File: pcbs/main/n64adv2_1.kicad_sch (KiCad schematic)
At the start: 74 parts, among them Q1 2N2222, Q2 2N2222, Q3 2N2222, U1 10M16SCE144/10M25SCE144, U2 ADV7513, U3 MT48LC16M16A2-TSOP54, U4 SI5356DIY, U5 ASE-50.000MHZ-LC-T, U6 ASE-24.576MHZ-LC-T, U7 2G17TI_DBV, X1 Conn_01x30, X2 2510-, X3 hdmi-con, X4 TEI0005, X5 USB3140-30-0170-0-C, Y41 7A-27.000MAAJ-T

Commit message: update main PCB with minor changes, e.g. ensure that solder mask bridges between 0.5mm pitched pads has min. 0.1mm thickness
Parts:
- ALRCLK1, ASCLK1, ASDATA1, CTRL1, VD0, VD1, VD2, VD3, VD4, VD5, VD6, VDCLK1, nRST1, nVDS1, nViDeBlur1: value (none) -> SMD1; footprint (none) -> n64adv2:SMD0,8-1,6
- D23: value (none) -> NUP4114; footprint (none) -> n64adv2:SOT-23-6
- SJ11, SJ31, SJ5, SJ6: value (none) -> SJSMALL; footprint (none) -> n64adv2:SJ_SMALL
- TP_SCL0, TP_SDA0, TP_SPDIF0: value (none) -> TPB1,27; footprint (none) -> n64adv2:B1,27
- U3: value MT48LC16M16A2-TSOP54 -> AS4C8M16SA-xTCN
- U4: value SI5356DIY -> SI5356A-B-GMR
- U7: value 2G17TI_DBV -> 74LVC2G17DBV
- X2: value 2510- -> 3020-10-0300-00

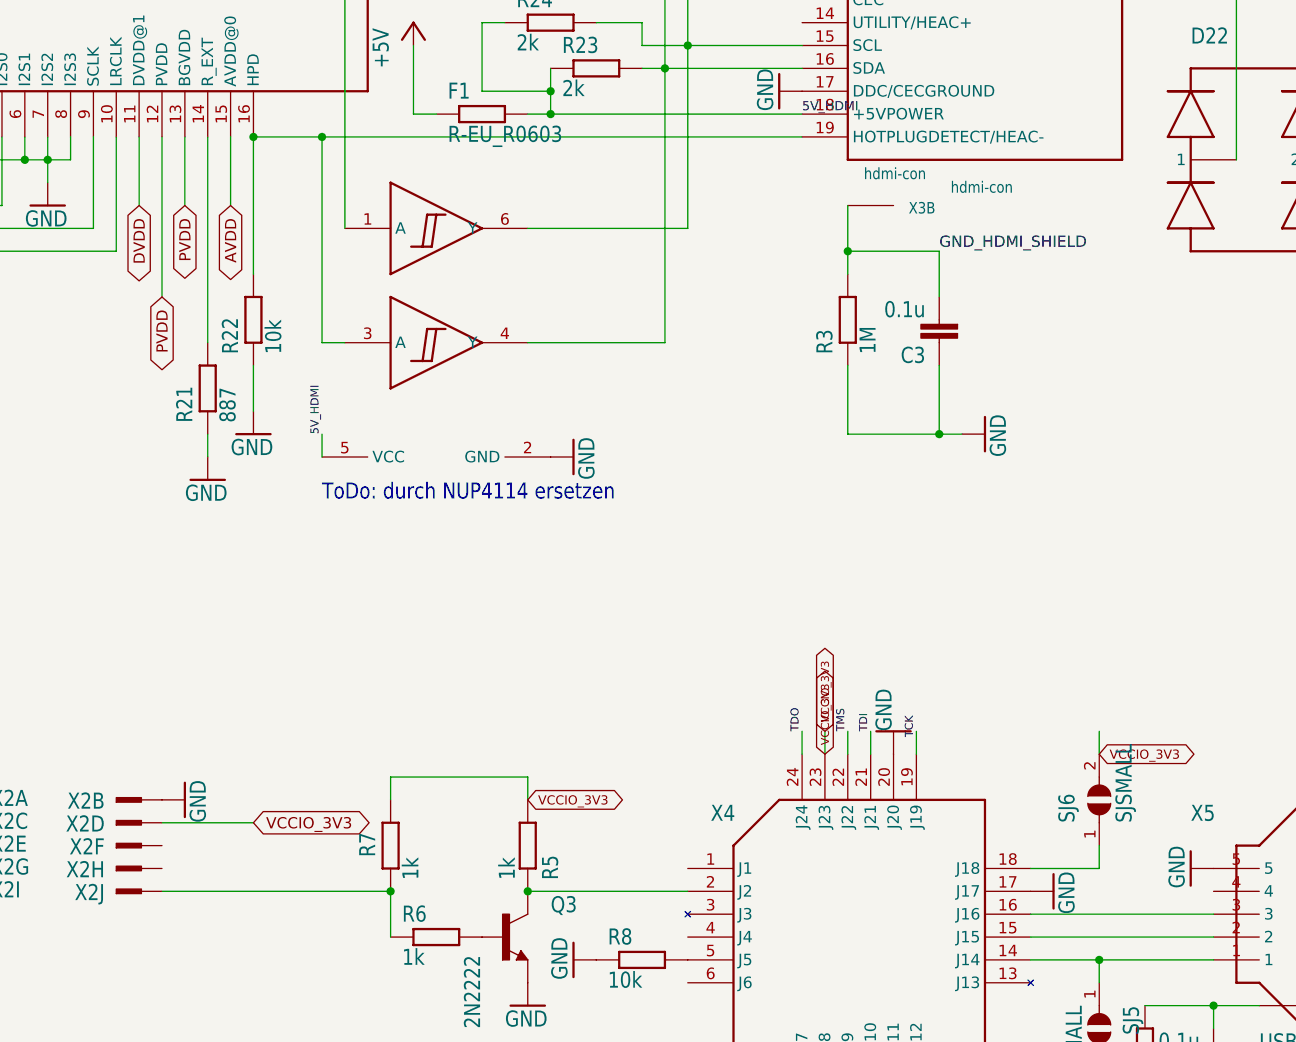
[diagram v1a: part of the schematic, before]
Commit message: update main PCB: - optimize some trace routing - optimize component selection/placing (e.g. HDMI port full SMD, JTAG as SMD alternative) - add license to silkscreen
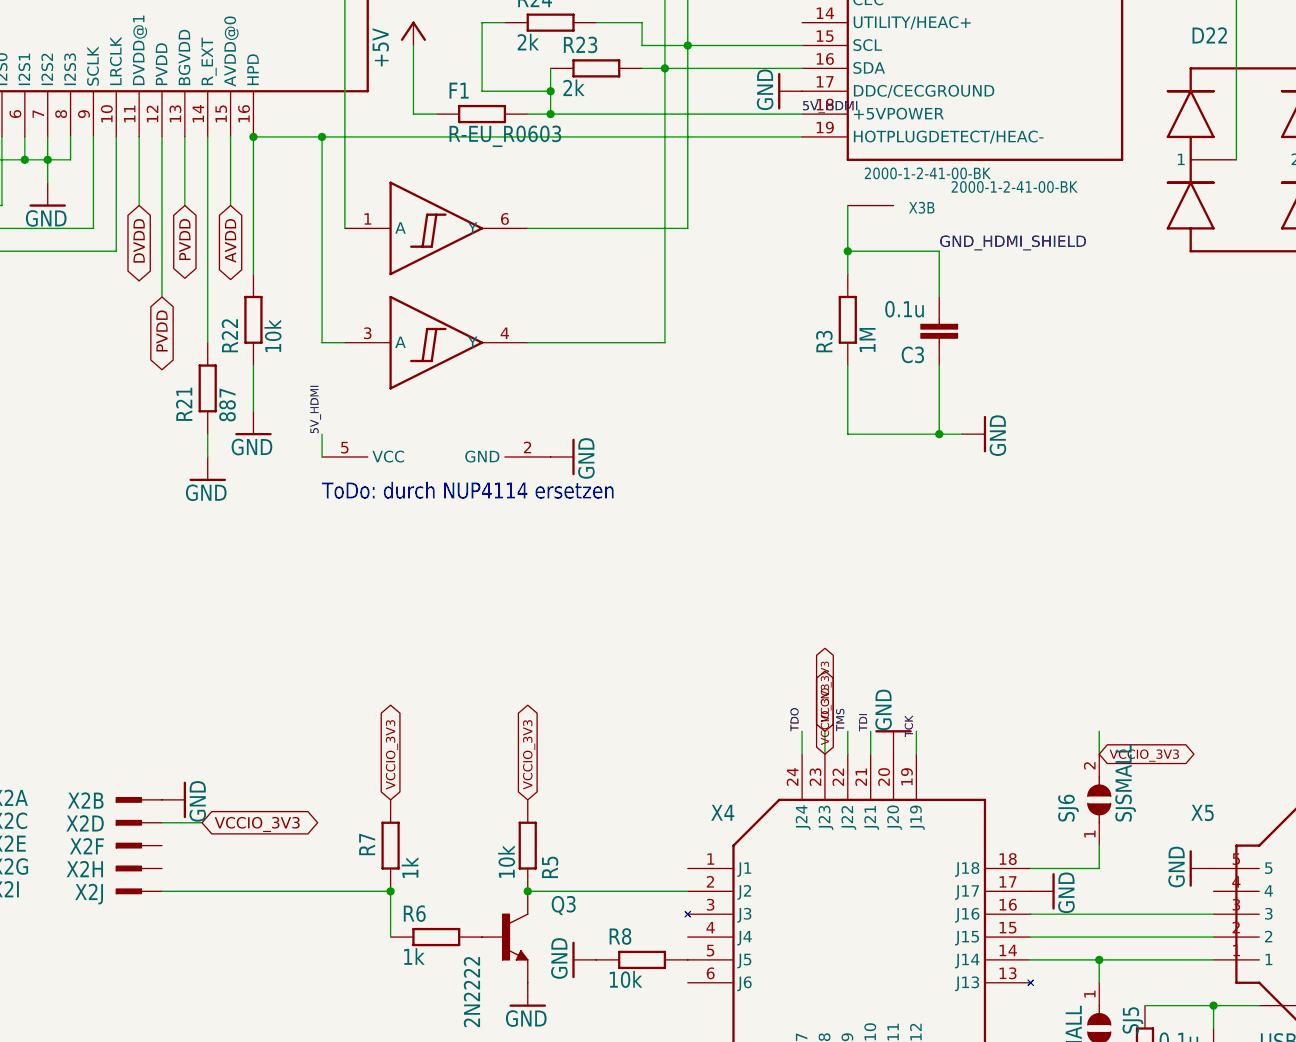
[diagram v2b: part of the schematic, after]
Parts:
- R5: value 1k -> 10k
- X3: value hdmi-con -> 2000-1-2-41-00-BK; footprint n64adv2:685119134923 -> n64adv2:hdmi_smd_shield_2000-1-2-41-00-BK
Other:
- company: (none) -> Peter 'borti4938' Bartmann
- title: (none) -> N64Adv2 (ADV7513)
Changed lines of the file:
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@@
 (kicad_sch (version 20211123) (generator eeschema)
   (paper "User" 783.336 357.353)
+  (title_block
+    (title "N64Adv2 (ADV7513)")
+    (rev "v20220729")
+    (company "Peter 'borti4938' Bartmann")
+    (comment 1 "Schematic and PCB (c) 2021, 2022 by Peter Bartmann")
+    (comment 2 "N64Adv2_20220729")
+    (comment 3 "Licensed under CERN-OHL-W v2")
+  )
   (junction (at 332.74 302.26) (diameter 0) (color 0 0 0 0)
   )
@@
     (stroke (width 0) (type default) (color 0 0 0 0))
   )
-  (wire (pts (xy 604.52 208.28) (xy 604.52 205.74))
-    (stroke (width 0) (type default) (color 0 0 0 0))
-  )
   (wire (pts (xy 292.1 231.14) (xy 320.04 231.14))
     (stroke (width 0) (type default) (color 0 0 0 0))
@@
     (stroke (width 0) (type default) (color 0 0 0 0))
   )
-  (wire (pts (xy 619.76 205.74) (xy 604.52 205.74))
-    (stroke (width 0) (type default) (color 0 0 0 0))
-  )
   (wire (pts (xy 655.32 147.32) (xy 655.32 142.24))
     (stroke (width 0) (type default) (color 0 0 0 0))
@@
     (stroke (width 0) (type default) (color 0 0 0 0))
   )
-  (wire (pts (xy 579.12 210.82) (xy 589.28 210.82))
-    (stroke (width 0) (type default) (color 0 0 0 0))
-  )
   (wire (pts (xy 563.88 60.96) (xy 563.88 33.02))
     (stroke (width 0) (type default) (color 0 0 0 0))
@@
     (stroke (width 0) (type default) (color 0 0 0 0))
   )
-  (wire (pts (xy 619.76 208.28) (xy 619.76 205.74))
-    (stroke (width 0) (type default) (color 0 0 0 0))
-  )
   (wire (pts (xy 683.26 203.2) (xy 683.26 200.66))
     (stroke (width 0) (type default) (color 0 0 0 0))
@@
     (stroke (width 0) (type default) (color 0 0 0 0))
   )
+  (wire (pts (xy 579.12 210.82) (xy 583.565 210.82))
+    (stroke (width 0) (type default) (color 0 0 0 0))
+  )
   (wire (pts (xy 205.74 111.76) (xy 198.12 111.76))
     (stroke (width 0) (type default) (color 0 0 0 0))
@@
     )
   )
-  (global_label "VCCIO_3V3" (shape bidirectional) (at 619.76 208.28 0) (fields_autoplaced)
+  (global_label "VCCIO_3V3" (shape bidirectional) (at 619.76 208.28 90) (fields_autoplaced)
     (effects (font (size 1.016 1.016)) (justify left))
-    (property "Intersheet References" "${INTERSHEET_REFS}" (id 0) (at 0 0 0)
+    (property "Intersheet References" "${INTERSHEET_REFS}" (id 0) (at 411.48 828.04 0)
       (effects (font (size 1.27 1.27)) hide)
     )
@@
     )
   )
+  (global_label "VCCIO_3V3" (shape bidirectional) (at 604.52 208.28 90) (fields_autoplaced)
+    (effects (font (size 1.016 1.016)) (justify left))
+    (property "Intersheet References" "${INTERSHEET_REFS}" (id 0) (at 396.24 828.04 0)
+      (effects (font (size 1.27 1.27)) hide)
+    )
+  )
   (global_label "U7_2V5" (shape bidirectional) (at 416.56 172.72 90) (fields_autoplaced)
     (effects (font (size 0.889 0.889)) (justify left))
@@
     )
   )
-  (global_label "VCCIO_3V3" (shape bidirectional) (at 589.28 210.82 0) (fields_autoplaced)
+  (global_label "VCCIO_3V3" (shape bidirectional) (at 583.565 210.82 0) (fields_autoplaced)
     (effects (font (size 1.2446 1.2446)) (justify left))
-    (property "Intersheet References" "${INTERSHEET_REFS}" (id 0) (at 0 0 0)
+    (property "Intersheet References" "${INTERSHEET_REFS}" (id 0) (at -5.715 0 0)
       (effects (font (size 1.27 1.27)) hide)
     )
@@
       (effects (font (size 1.27 1.0795)) (justify left bottom))
     )
-    (property "Value" "hdmi-con" (id 1) (at 666.75 140.97 0)
+    (property "Value" "2000-1-2-41-00-BK" (id 1) (at 666.75 140.97 0)
       (effects (font (size 1.27 1.0795)) (justify left bottom))
     )
-    (property "Footprint" "n64adv2:685119134923" (id 2) (at 670.56 111.76 0)
+    (property "Footprint" "n64adv2:hdmi_smd_shield_2000-1-2-41-00-BK" (id 2) (at 670.56 111.76 0)
       (effects (font (size 1.27 1.27)) hide)
     )
@@
       (effects (font (size 1.27 1.0795)) (justify left bottom))
     )
-    (property "Value" "hdmi-con" (id 1) (at 657.1 139.46 0)
+    (property "Value" "2000-1-2-41-00-BK" (id 1) (at 657.1 139.46 0)
       (effects (font (size 1.27 1.0795)) (justify left bottom))
     )
-    (property "Footprint" "n64adv2:685119134923" (id 2) (at 660.4 142.24 0)
+    (property "Footprint" "n64adv2:hdmi_smd_shield_2000-1-2-41-00-BK" (id 2) (at 660.4 142.24 0)
       (effects (font (size 1.27 1.27)) hide)
     )
@@
       (effects (font (size 1.778 1.5113)) (justify left bottom))
     )
-    (property "Value" "1k" (id 1) (at 616.458 217.17 0)
+    (property "Value" "10k" (id 1) (at 616.458 217.17 0)
       (effects (font (size 1.778 1.5113)) (justify left bottom))
     )

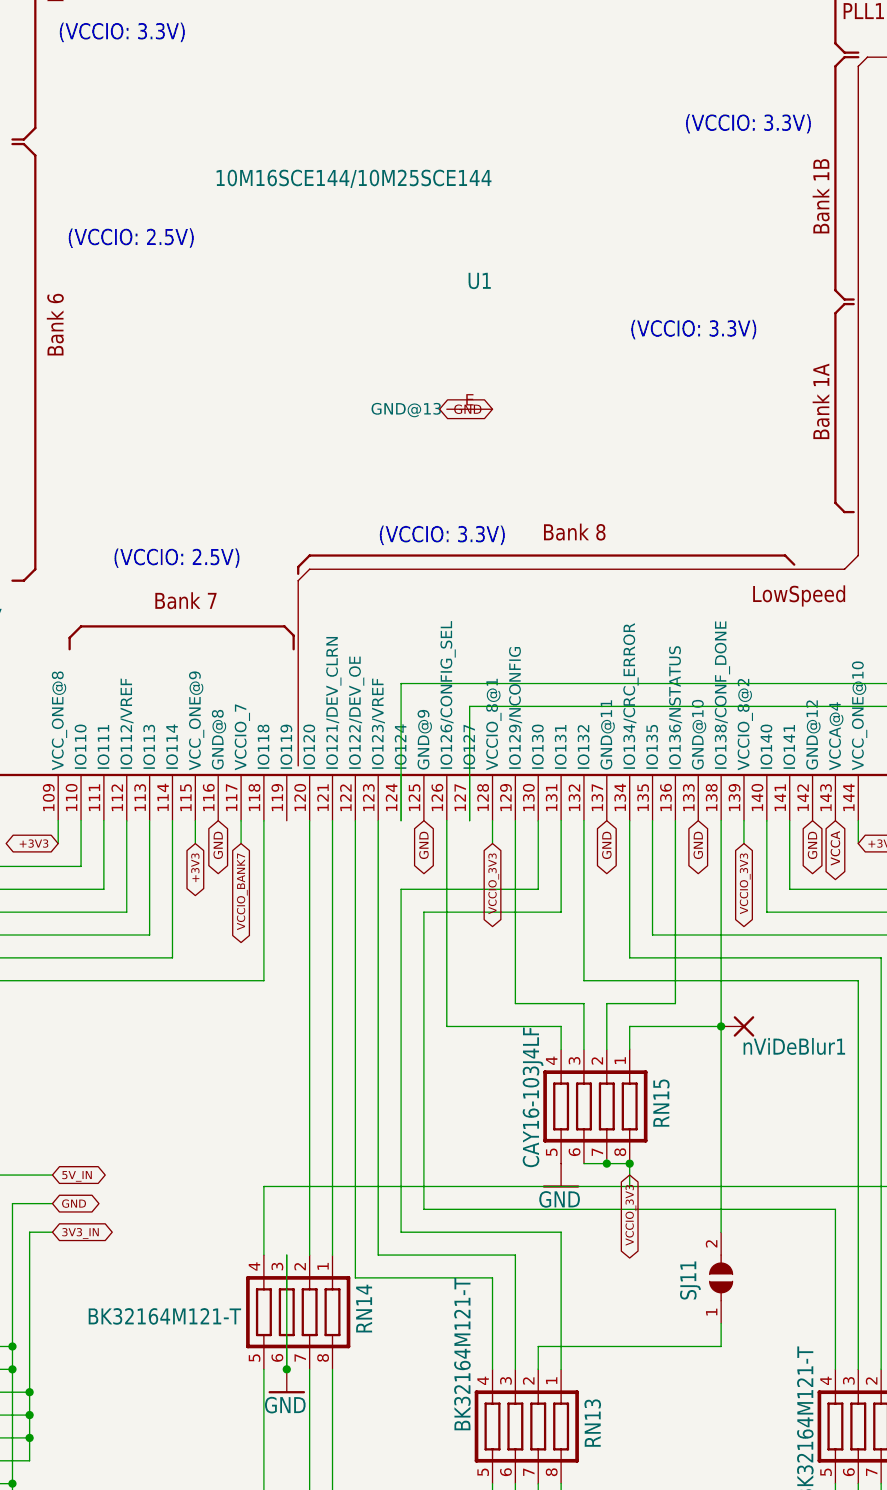
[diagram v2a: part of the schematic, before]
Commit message: Main PCB update: - edge cuts: yet another update hopefully getting the perfect fit this time - hdmi connector position moved 0.5mm to the left - optimize mask for D21, D22, X3
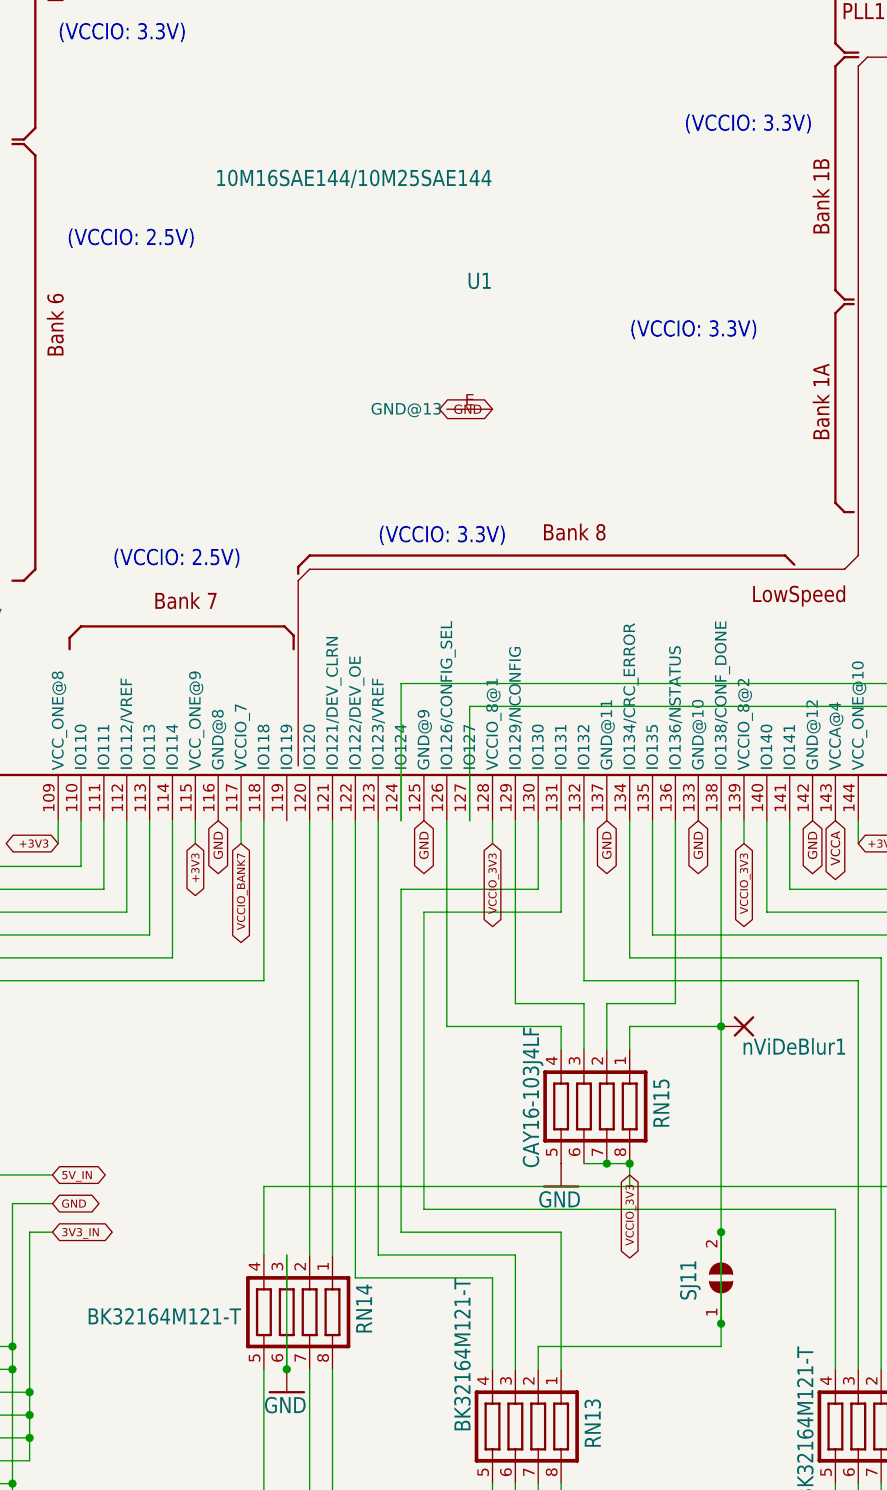
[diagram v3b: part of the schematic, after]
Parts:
- U1: value 10M16SCE144/10M25SCE144 -> 10M16SAE144/10M25SAE144
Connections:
- net at RN13.2, SJ11.1: now also RN15.1, SJ11.2, U1.138 (IO138/CONF_DONE), nViDeBlur1.P$1 (P)
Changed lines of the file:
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@@
   (junction (at 464.82 195.58) (diameter 0) (color 0 0 0 0)
   )
+  (junction (at 302.26 271.78) (diameter 0) (color 0 0 0 0)
+  )
   (junction (at 558.8 137.16) (diameter 0) (color 0 0 0 0)
   )
@@
   (junction (at 314.96 314.96) (diameter 0) (color 0 0 0 0)
   )
+  (junction (at 302.26 261.62) (diameter 0) (color 0 0 0 0)
+  )
   (junction (at 546.1 218.44) (diameter 0) (color 0 0 0 0)
   )
@@
     (stroke (width 0) (type default) (color 0 0 0 0))
   )
+  (wire (pts (xy 302.26 261.62) (xy 302.26 271.78))
+    (stroke (width 0) (type default) (color 0 0 0 0))
+  )
   (wire (pts (xy 200.66 116.84) (xy 205.74 116.84))
     (stroke (width 0) (type default) (color 0 0 0 0))
@@
       (effects (font (size 1.778 1.5113)) (justify left bottom))
     )
-    (property "Value" "10M16SCE144/10M25SCE144" (id 1) (at 276.86 143.51 0)
+    (property "Value" "10M16SAE144/10M25SAE144" (id 1) (at 276.86 143.51 0)
       (effects (font (size 1.778 1.5113)) (justify left bottom))
     )

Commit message: some BOM updates
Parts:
- D23: value NUP4114 -> NUP4114HMR6T1G
- F1: value R-EU_R0603 -> MF-FSMF020X-2
- X1: value Conn_01x30 -> 3-1734592-0
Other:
- note added: "ToDo: wrong symbol, replace with NUP4114 symbol"
- note removed: "ToDo: durch NUP4114 ersetzen"
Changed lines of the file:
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@@
     (effects (font (size 1.778 1.5113)) (justify left bottom))
   )
-  (text "ToDo: durch NUP4114 ersetzen" (at 596.9 175.26 180)
+  (text "ToDo: wrong symbol,\n      replace with NUP4114 symbol"
+    (at 597.535 179.705 0)
     (effects (font (size 1.778 1.5113)) (justify left bottom))
   )
@@
       (effects (font (size 1.27 1.27)) hide)
     )
-    (property "Value" "NUP4114" (id 1) (at 607.06 152.4 0)
+    (property "Value" "NUP4114HMR6T1G" (id 1) (at 607.06 152.4 0)
       (effects (font (size 1.27 1.27)) hide)
     )
@@
     (in_bom yes) (on_board yes) (fields_autoplaced)
     (property "Reference" "X1" (id 0) (at 212.09 259.715 0))
-    (property "Value" "Conn_01x30" (id 1) (at 212.09 262.255 0))
+    (property "Value" "3-1734592-0" (id 1) (at 212.09 262.255 0))
     (property "Footprint" "n64adv2:FH12-30S-0.5SH" (id 2) (at 212.09 304.8 0)
       (effects (font (size 1.27 1.27)) hide)
@@
       (effects (font (size 1.778 1.5113)) (justify left bottom))
     )
-    (property "Value" "R-EU_R0603" (id 1) (at 610.87 135.382 0)
+    (property "Value" "MF-FSMF020X-2" (id 1) (at 610.87 135.382 0)
       (effects (font (size 1.778 1.5113)) (justify left bottom))
     )
@@
       (effects (font (size 1.27 1.27)) hide)
     )
-    (property "Value" "NUP4114" (id 1) (at 609.6 170.18 0)
+    (property "Value" "NUP4114HMR6T1G" (id 1) (at 609.6 170.18 0)
       (effects (font (size 1.27 1.27)) hide)
     )
@@
       (effects (font (size 1.27 1.27)) hide)
     )
-    (property "Value" "NUP4114" (id 1) (at 607.06 165.1 0)
-      (effects (font (size 1.27 1.27)) hide)
-    )
+    (property "Value" "NUP4114HMR6T1G" (id 1) (at 607.06 165.1 0)
+      (effects (font (size 1.27 1.27)) hide)
+    )
